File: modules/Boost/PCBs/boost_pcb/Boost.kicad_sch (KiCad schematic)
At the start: 28 parts, among them J1 2x5 IDC, J2 THONKICONN, J3 THONKICONN, Q1 2N3904, U1 TL074

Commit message: Moved PCB
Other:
- note added: "Scale-down Amp Variable gain 1/10x to 2x"
- note removed: "Scale-down Amp Gain 1/10 to 2x"
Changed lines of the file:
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@@
 		)
 	)
-	(text "Scale-down Amp\nGain 1/10 to 2x"
+	(text "Scale-down Amp\nVariable gain 1/10x to 2x"
 		(exclude_from_sim no)
 		(at 91.44 36.83 0)

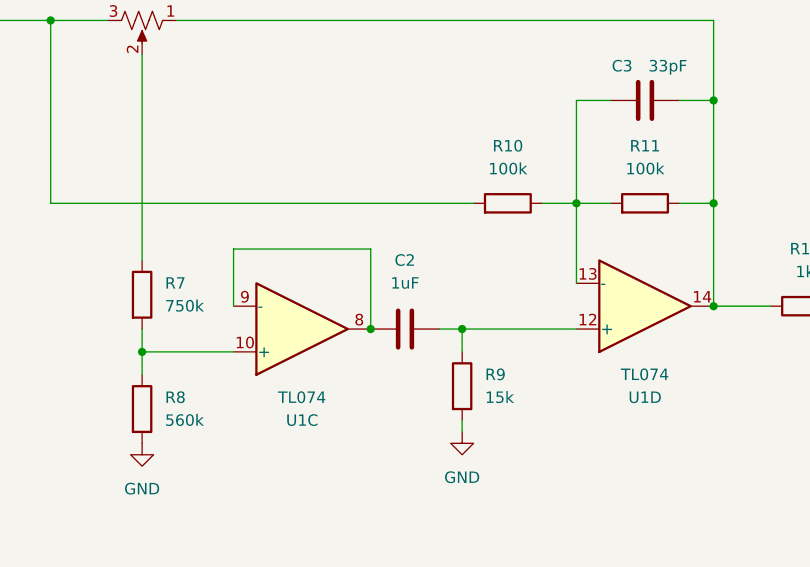
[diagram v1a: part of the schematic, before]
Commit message: Add boost BoM
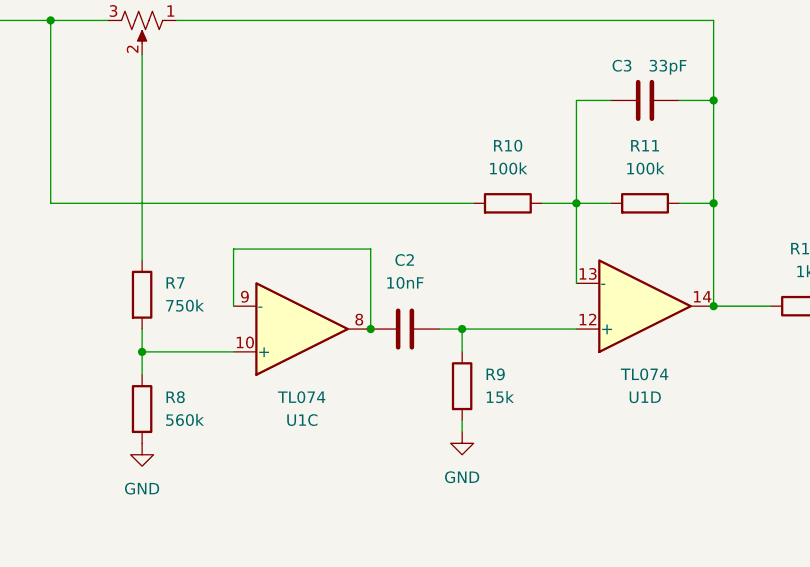
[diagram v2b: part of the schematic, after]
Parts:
- C2: value 1uF -> 10nF
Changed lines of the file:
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@@
 			)
 		)
-		(property "Value" "1uF"
+		(property "Value" "10nF"
 			(at 208.28 93.98 90)
 			(effects

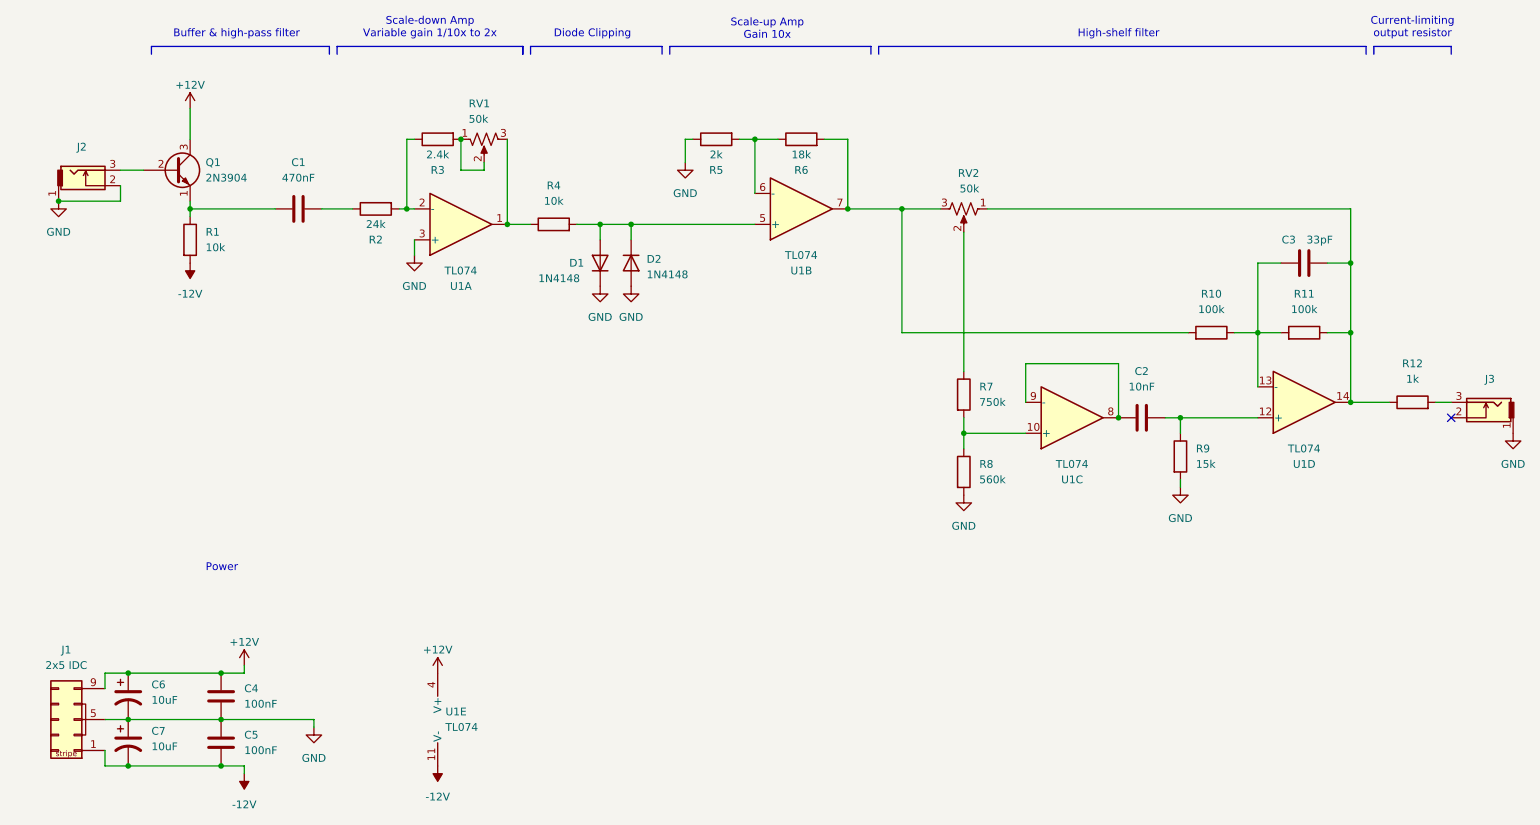
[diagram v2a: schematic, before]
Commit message: Flip boost pots
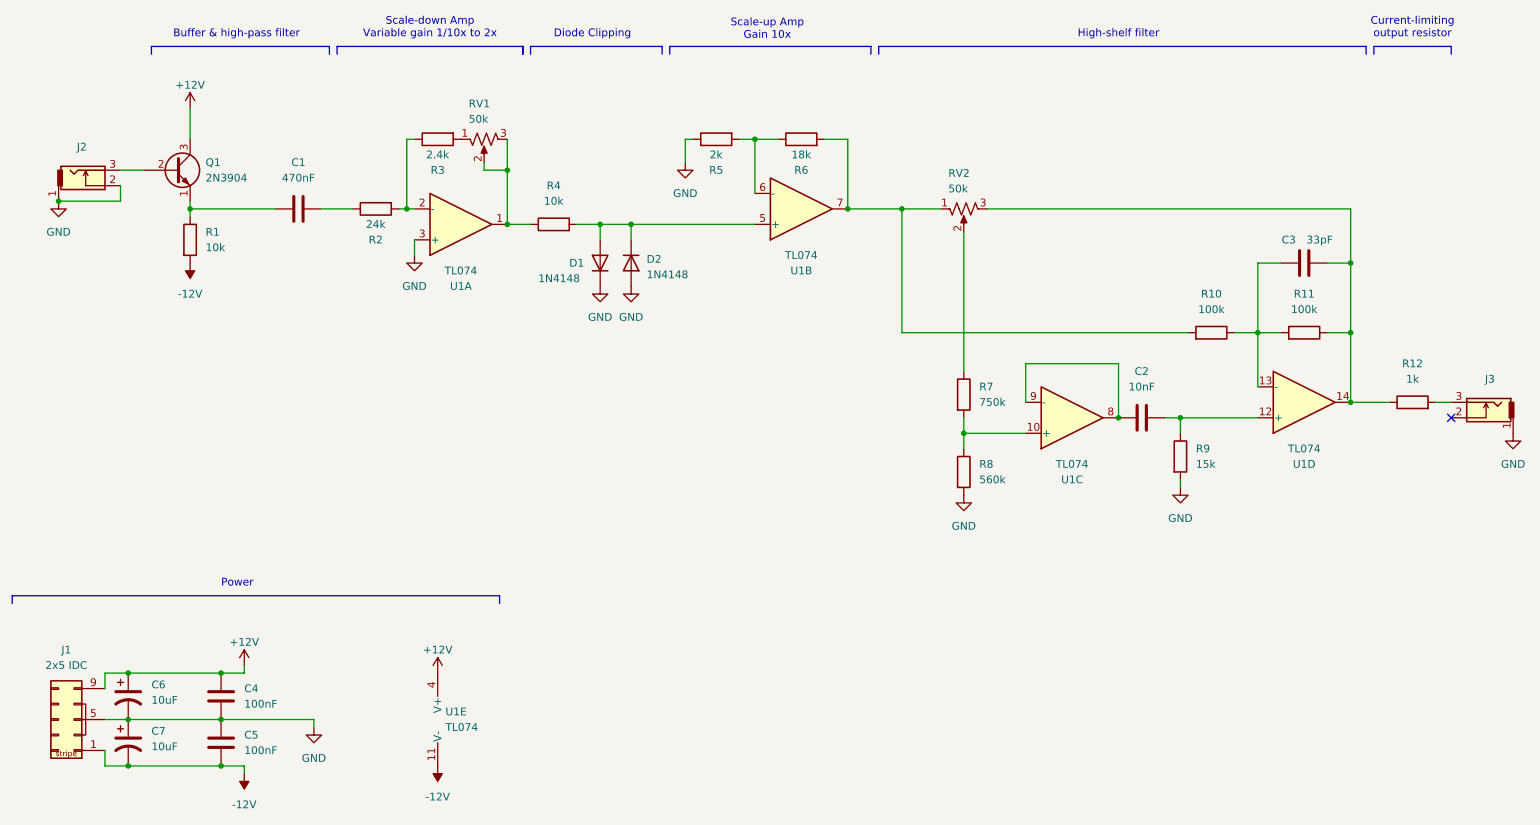
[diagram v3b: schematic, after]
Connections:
- net at C3.2, R11.1, R12.1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: now also RV2.3; no longer RV2.1
- net at R10.2, R6.2, U1.7: now also RV2.1; no longer RV2.3
- net at R3.2, RV1.1: no longer RV1.2
- net at R4.1, RV1.3, U1.1: now also RV1.2
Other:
- moved on the sheet: RV2
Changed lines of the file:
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@@
 		(title "Boost")
 		(date "2024-09-14")
-		(rev "1.0")
+		(rev "1.1")
 		(company "Free Modular")
 	)
@@
 	)
 	(junction
+		(at 104.14 58.42)
+		(diameter 0)
+		(color 0 0 0 0)
+	)
+	(junction
 		(at 52.07 64.77)
 		(diameter 0)
@@
 	(junction
 		(at 160.02 64.77)
-		(diameter 0)
-		(color 0 0 0 0)
-	)
-	(junction
-		(at 96.52 53.34)
 		(diameter 0)
 		(color 0 0 0 0)
@@
 	(wire
 		(pts
-			(xy 104.14 53.34) (xy 104.14 67.31)
+			(xy 104.14 53.34) (xy 104.14 58.42)
 		)
 		(stroke
@@
 		)
 	)
+	(polyline
+		(pts
+			(xy 22.86 129.54) (xy 22.86 128.27)
+		)
+		(stroke
+			(width 0)
+			(type default)
+		)
+	)
 	(wire
 		(pts
@@
 	(wire
 		(pts
+			(xy 104.14 58.42) (xy 104.14 67.31)
+		)
+		(stroke
+			(width 0)
+			(type default)
+		)
+	)
+	(wire
+		(pts
 			(xy 179.07 104.14) (xy 179.07 101.6)
 		)
@@
 	(wire
 		(pts
-			(xy 96.52 58.42) (xy 100.33 58.42)
-		)
-		(stroke
-			(width 0)
-			(type default)
-		)
-	)
-	(wire
-		(pts
 			(xy 168.91 85.09) (xy 215.9 85.09)
 		)
@@
 	(wire
 		(pts
+			(xy 100.33 58.42) (xy 104.14 58.42)
+		)
+		(stroke
+			(width 0)
+			(type default)
+		)
+	)
+	(wire
+		(pts
 			(xy 124.46 67.31) (xy 124.46 69.85)
 		)
@@
 		)
 	)
+	(polyline
+		(pts
+			(xy 22.86 128.27) (xy 102.87 128.27)
+		)
+		(stroke
+			(width 0)
+			(type default)
+		)
+	)
 	(wire
 		(pts
@@
 	(wire
 		(pts
-			(xy 96.52 53.34) (xy 96.52 58.42)
-		)
-		(stroke
-			(width 0)
-			(type default)
-		)
-	)
-	(wire
-		(pts
 			(xy 87.63 64.77) (xy 87.63 53.34)
 		)
@@
 		(pts
 			(xy 165.1 39.37) (xy 165.1 38.1)
+		)
+		(stroke
+			(width 0)
+			(type default)
+		)
+	)
+	(polyline
+		(pts
+			(xy 102.87 128.27) (xy 102.87 129.54)
 		)
 		(stroke
@@
 	(text "Power"
 		(exclude_from_sim no)
-		(at 54.61 124.46 0)
+		(at 57.15 127 0)
 		(effects
 			(font
@@
 	(symbol
 		(lib_id "Device:R_Potentiometer_US")
-		(at 179.07 64.77 270)
+		(at 179.07 64.77 90)
+		(mirror x)
 		(unit 1)
 		(exclude_from_sim no)
@@
 		(dnp no)
 		(property "Reference" "RV2"
-			(at 181.61 58.928 90)
+			(at 176.53 58.928 90)
 			(effects
 				(font
@@
 		)
 		(property "Value" "50k"
-			(at 181.61 61.468 90)
-			(effects
-				(font
+			(at 176.53 61.468 90)
+			(effects
+				(font
